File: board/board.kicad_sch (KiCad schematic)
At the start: 4 parts, among them J1 0xx_LED, J2 0xx_LED

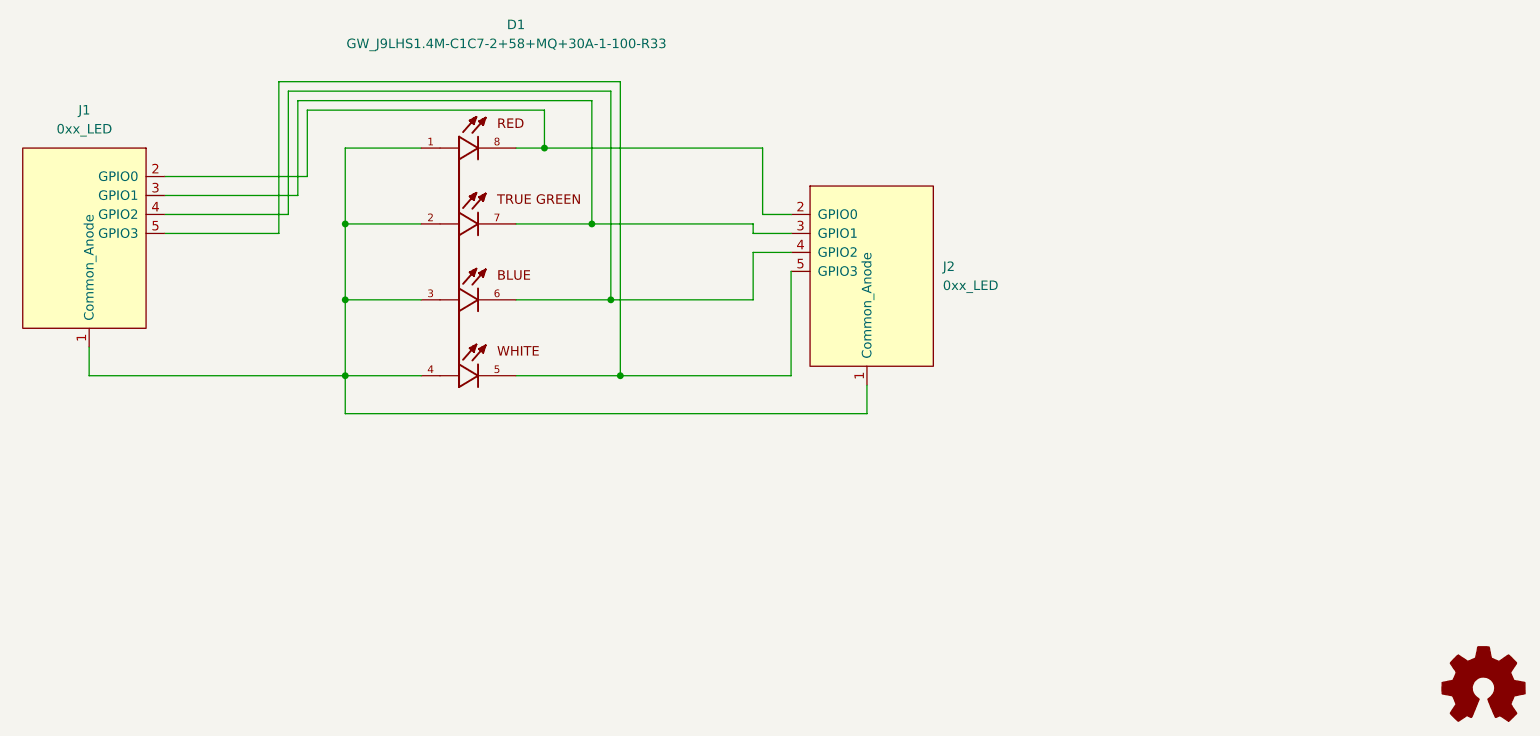
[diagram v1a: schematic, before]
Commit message: Update Layout | Remove DRC Errors | Connected unused Edgy Pins
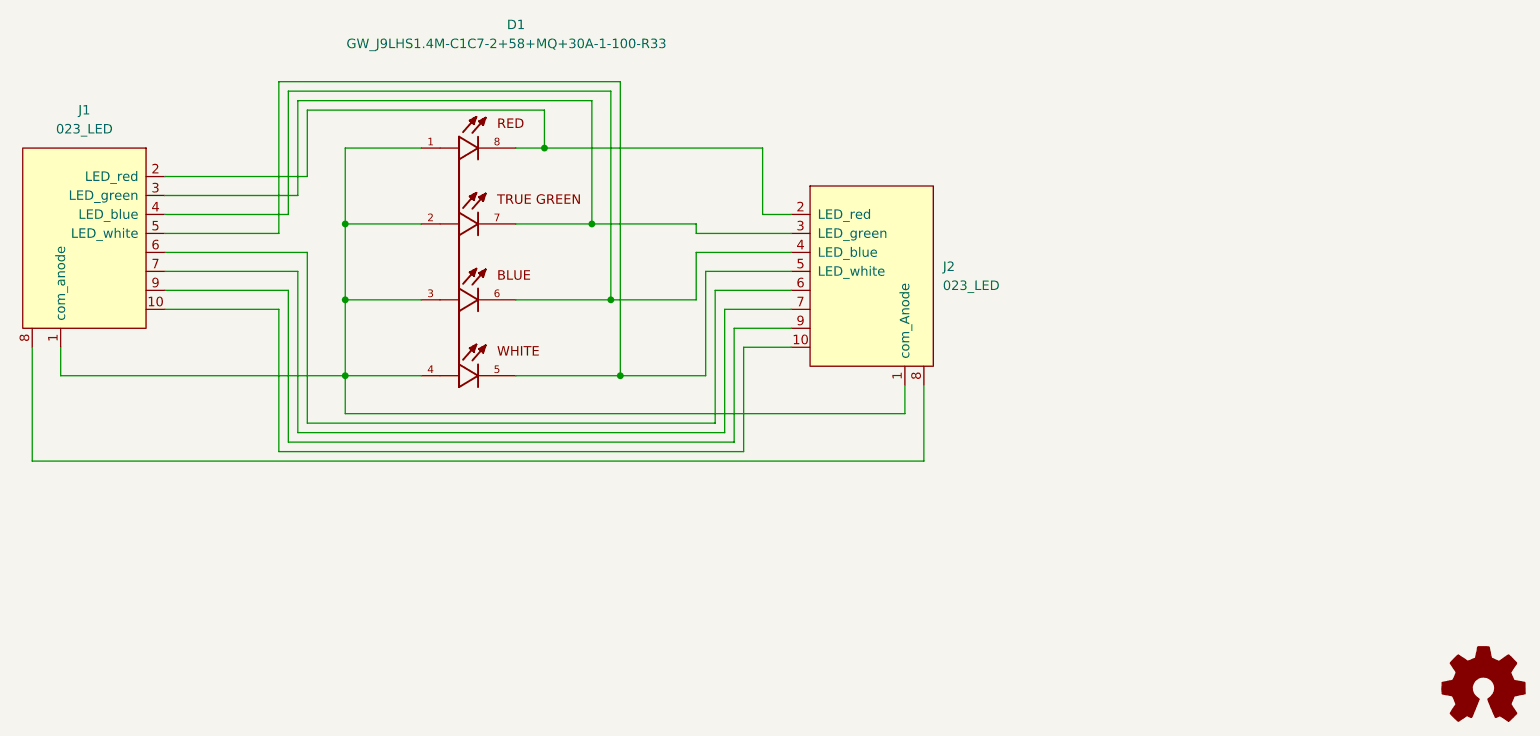
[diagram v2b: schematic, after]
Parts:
- J1, J2: value 0xx_LED -> 023_LED
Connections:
- new net: J1.10, J2.10
- new net: J1.6, J2.6
- new net: J1.7, J2.7
- new net: J1.8, J2.8
- new net: J1.9, J2.9
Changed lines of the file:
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@@
   (junction (at 153.67 95.25) (diameter 0) (color 0 0 0 0)
   )
+  (junction (at 157.48 115.57) (diameter 0) (color 0 0 0 0)
+  )
   (junction (at 147.32 85.09) (diameter 0) (color 0 0 0 0)
   )
   (junction (at 120.65 105.41) (diameter 0) (color 0 0 0 0)
   )
-  (junction (at 157.48 115.57) (diameter 0) (color 0 0 0 0)
-  )
-  (wire (pts (xy 86.36 115.57) (xy 120.65 115.57))
+  (wire (pts (xy 96.52 99.06) (xy 115.57 99.06))
+    (stroke (width 0) (type default) (color 0 0 0 0))
+  )
+  (wire (pts (xy 82.55 115.57) (xy 120.65 115.57))
+    (stroke (width 0) (type default) (color 0 0 0 0))
+  )
+  (wire (pts (xy 168.91 101.6) (xy 180.34 101.6))
     (stroke (width 0) (type default) (color 0 0 0 0))
   )
@@
     (stroke (width 0) (type default) (color 0 0 0 0))
   )
+  (wire (pts (xy 172.72 124.46) (xy 172.72 109.22))
+    (stroke (width 0) (type default) (color 0 0 0 0))
+  )
   (wire (pts (xy 147.32 85.09) (xy 147.32 80.01))
     (stroke (width 0) (type default) (color 0 0 0 0))
@@
     (stroke (width 0) (type default) (color 0 0 0 0))
   )
-  (wire (pts (xy 190.5 116.84) (xy 190.5 120.65))
+  (wire (pts (xy 195.58 116.84) (xy 195.58 120.65))
+    (stroke (width 0) (type default) (color 0 0 0 0))
+  )
+  (wire (pts (xy 115.57 121.92) (xy 170.18 121.92))
     (stroke (width 0) (type default) (color 0 0 0 0))
   )
@@
     (stroke (width 0) (type default) (color 0 0 0 0))
   )
-  (wire (pts (xy 180.34 96.52) (xy 175.26 96.52))
+  (wire (pts (xy 168.91 101.6) (xy 168.91 115.57))
+    (stroke (width 0) (type default) (color 0 0 0 0))
+  )
+  (wire (pts (xy 180.34 96.52) (xy 167.64 96.52))
     (stroke (width 0) (type default) (color 0 0 0 0))
   )
@@
     (stroke (width 0) (type default) (color 0 0 0 0))
   )
-  (wire (pts (xy 180.34 99.06) (xy 175.26 99.06))
+  (wire (pts (xy 180.34 99.06) (xy 167.64 99.06))
     (stroke (width 0) (type default) (color 0 0 0 0))
   )
@@
     (stroke (width 0) (type default) (color 0 0 0 0))
   )
-  (wire (pts (xy 175.26 95.25) (xy 153.67 95.25))
+  (wire (pts (xy 167.64 95.25) (xy 153.67 95.25))
+    (stroke (width 0) (type default) (color 0 0 0 0))
+  )
+  (wire (pts (xy 172.72 109.22) (xy 180.34 109.22))
     (stroke (width 0) (type default) (color 0 0 0 0))
   )
@@
     (stroke (width 0) (type default) (color 0 0 0 0))
   )
-  (wire (pts (xy 180.34 115.57) (xy 157.48 115.57))
-    (stroke (width 0) (type default) (color 0 0 0 0))
-  )
-  (wire (pts (xy 120.65 120.65) (xy 190.5 120.65))
+  (wire (pts (xy 120.65 120.65) (xy 195.58 120.65))
     (stroke (width 0) (type default) (color 0 0 0 0))
   )
@@
     (stroke (width 0) (type default) (color 0 0 0 0))
   )
+  (wire (pts (xy 96.52 104.14) (xy 113.03 104.14))
+    (stroke (width 0) (type default) (color 0 0 0 0))
+  )
+  (wire (pts (xy 114.3 123.19) (xy 114.3 101.6))
+    (stroke (width 0) (type default) (color 0 0 0 0))
+  )
+  (wire (pts (xy 113.03 104.14) (xy 113.03 124.46))
+    (stroke (width 0) (type default) (color 0 0 0 0))
+  )
   (wire (pts (xy 130.81 85.09) (xy 120.65 85.09))
     (stroke (width 0) (type default) (color 0 0 0 0))
   )
+  (wire (pts (xy 171.45 123.19) (xy 114.3 123.19))
+    (stroke (width 0) (type default) (color 0 0 0 0))
+  )
   (wire (pts (xy 176.53 93.98) (xy 176.53 85.09))
     (stroke (width 0) (type default) (color 0 0 0 0))
   )
+  (wire (pts (xy 115.57 99.06) (xy 115.57 121.92))
+    (stroke (width 0) (type default) (color 0 0 0 0))
+  )
+  (wire (pts (xy 78.74 127) (xy 198.12 127))
+    (stroke (width 0) (type default) (color 0 0 0 0))
+  )
   (wire (pts (xy 96.52 91.44) (xy 114.3 91.44))
     (stroke (width 0) (type default) (color 0 0 0 0))
   )
+  (wire (pts (xy 198.12 127) (xy 198.12 116.84))
+    (stroke (width 0) (type default) (color 0 0 0 0))
+  )
+  (wire (pts (xy 180.34 104.14) (xy 170.18 104.14))
+    (stroke (width 0) (type default) (color 0 0 0 0))
+  )
+  (wire (pts (xy 111.76 125.73) (xy 111.76 106.68))
+    (stroke (width 0) (type default) (color 0 0 0 0))
+  )
   (wire (pts (xy 180.34 93.98) (xy 176.53 93.98))
     (stroke (width 0) (type default) (color 0 0 0 0))
   )
+  (wire (pts (xy 78.74 111.76) (xy 78.74 127))
+    (stroke (width 0) (type default) (color 0 0 0 0))
+  )
   (wire (pts (xy 114.3 78.74) (xy 153.67 78.74))
     (stroke (width 0) (type default) (color 0 0 0 0))
@@
     (stroke (width 0) (type default) (color 0 0 0 0))
   )
-  (wire (pts (xy 175.26 96.52) (xy 175.26 95.25))
+  (wire (pts (xy 167.64 96.52) (xy 167.64 95.25))
+    (stroke (width 0) (type default) (color 0 0 0 0))
+  )
+  (wire (pts (xy 173.99 111.76) (xy 173.99 125.73))
     (stroke (width 0) (type default) (color 0 0 0 0))
   )
@@
     (stroke (width 0) (type default) (color 0 0 0 0))
   )
-  (wire (pts (xy 180.34 101.6) (xy 180.34 115.57))
-    (stroke (width 0) (type default) (color 0 0 0 0))
-  )
-  (wire (pts (xy 86.36 111.76) (xy 86.36 115.57))
+  (wire (pts (xy 114.3 101.6) (xy 96.52 101.6))
+    (stroke (width 0) (type default) (color 0 0 0 0))
+  )
+  (wire (pts (xy 82.55 111.76) (xy 82.55 115.57))
     (stroke (width 0) (type default) (color 0 0 0 0))
   )
@@
     (stroke (width 0) (type default) (color 0 0 0 0))
   )
+  (wire (pts (xy 173.99 125.73) (xy 111.76 125.73))
+    (stroke (width 0) (type default) (color 0 0 0 0))
+  )
   (wire (pts (xy 156.21 105.41) (xy 156.21 77.47))
     (stroke (width 0) (type default) (color 0 0 0 0))
@@
     (stroke (width 0) (type default) (color 0 0 0 0))
   )
+  (wire (pts (xy 170.18 104.14) (xy 170.18 121.92))
+    (stroke (width 0) (type default) (color 0 0 0 0))
+  )
+  (wire (pts (xy 171.45 106.68) (xy 171.45 123.19))
+    (stroke (width 0) (type default) (color 0 0 0 0))
+  )
   (wire (pts (xy 115.57 80.01) (xy 115.57 88.9))
     (stroke (width 0) (type default) (color 0 0 0 0))
   )
+  (wire (pts (xy 111.76 106.68) (xy 96.52 106.68))
+    (stroke (width 0) (type default) (color 0 0 0 0))
+  )
   (wire (pts (xy 147.32 80.01) (xy 115.57 80.01))
     (stroke (width 0) (type default) (color 0 0 0 0))
@@
     (stroke (width 0) (type default) (color 0 0 0 0))
   )
-  (wire (pts (xy 175.26 99.06) (xy 175.26 105.41))
+  (wire (pts (xy 167.64 99.06) (xy 167.64 105.41))
+    (stroke (width 0) (type default) (color 0 0 0 0))
+  )
+  (wire (pts (xy 180.34 106.68) (xy 171.45 106.68))
     (stroke (width 0) (type default) (color 0 0 0 0))
   )
@@
     (stroke (width 0) (type default) (color 0 0 0 0))
   )
+  (wire (pts (xy 168.91 115.57) (xy 157.48 115.57))
+    (stroke (width 0) (type default) (color 0 0 0 0))
+  )
+  (wire (pts (xy 113.03 124.46) (xy 172.72 124.46))
+    (stroke (width 0) (type default) (color 0 0 0 0))
+  )
   (wire (pts (xy 120.65 95.25) (xy 130.81 95.25))
     (stroke (width 0) (type default) (color 0 0 0 0))
@@
     (stroke (width 0) (type default) (color 0 0 0 0))
   )
-  (wire (pts (xy 175.26 105.41) (xy 156.21 105.41))
+  (wire (pts (xy 167.64 105.41) (xy 156.21 105.41))
+    (stroke (width 0) (type default) (color 0 0 0 0))
+  )
+  (wire (pts (xy 180.34 111.76) (xy 173.99 111.76))
     (stroke (width 0) (type default) (color 0 0 0 0))
   )
@@
     (in_bom yes) (on_board yes) (fields_autoplaced)
     (property "Reference" "J1" (id 0) (at 85.725 80.01 0))
-    (property "Value" "0xx_LED" (id 1) (at 85.725 82.55 0))
+    (property "Value" "023_LED" (id 1) (at 85.725 82.55 0))
     (property "Footprint" "on_edge:on_edge_2x05_device" (id 2) (at 77.47 81.28 0)
       (effects (font (size 1.27 1.27)) hide)
@@
     (pin "4")
     (pin "5")
+    (pin "8")
+    (pin "6")
+    (pin "7")
+    (pin "9")
+    (pin "10")
   )
   (symbol (lib_id "put_on_edge:011_GPIO") (at 191.77 102.87 0) (unit 1)
@@
       (effects (font (size 1.27 1.27)) (justify left))
     )
-    (property "Value" "0xx_LED" (id 1) (at 200.66 103.5049 0)
+    (property "Value" "023_LED" (id 1) (at 200.66 103.5049 0)
       (effects (font (size 1.27 1.27)) (justify left))
     )
@@
     )
     (pin "1")
+    (pin "10")
     (pin "2")
     (pin "3")
     (pin "4")
     (pin "5")
+    (pin "6")
+    (pin "7")
+    (pin "8")
+    (pin "9")
   )
   (symbol (lib_id "GW_J9LHS1.4M-C1C7-2_58_MQ_30A-1-100-R33:GW_J9LHS1.4M-C1C7-2+58+MQ+30A-1-100-R33") (at 138.43 100.33 0) (unit 1)
@@
     )
     (path "/02ab4736-fba1-4e6c-abef-aa7c088d94a7"
-      (reference "J1") (unit 1) (value "0xx_LED") (footprint "on_edge:on_edge_2x05_device")
+      (reference "J1") (unit 1) (value "023_LED") (footprint "on_edge:on_edge_2x05_device")
     )
     (path "/6169c5fa-dc29-45cd-8d2f-b575e54f7735"
-      (reference "J2") (unit 1) (value "0xx_LED") (footprint "on_edge:on_edge_2x05_host")
+      (reference "J2") (unit 1) (value "023_LED") (footprint "on_edge:on_edge_2x05_host")
     )
     (path "/b72b6f4a-7489-40f2-bb90-d75ae01aa368"

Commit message: Change edgy connector back to GPIO | Began adding Resistor to specific voltage
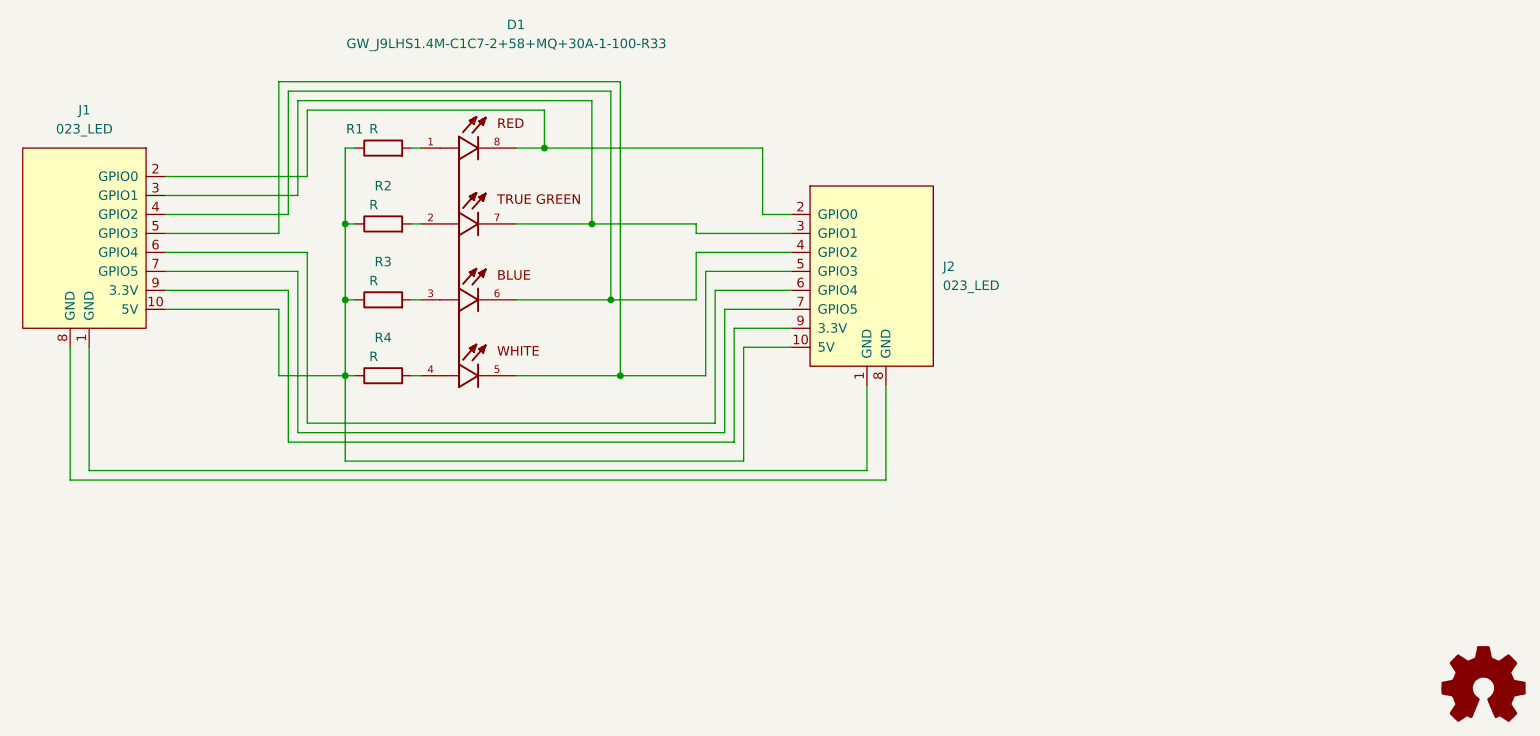
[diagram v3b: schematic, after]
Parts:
- added R1, R2, R3, R4: R, Resistor_SMD:R_0603_1608Metric_Pad0.98x0.95mm_HandSolder, symbol Device:R
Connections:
- net at J1.10 (5V), J2.10 (5V): now also R1.1, R2.1, R3.1, R4.1
- new net: J1.1 (GND), J2.1 (GND)
- new net: D1.3, R3.2
- new net: D1.1, R1.2
- new net: D1.2, R2.2
- new net: D1.4, R4.2

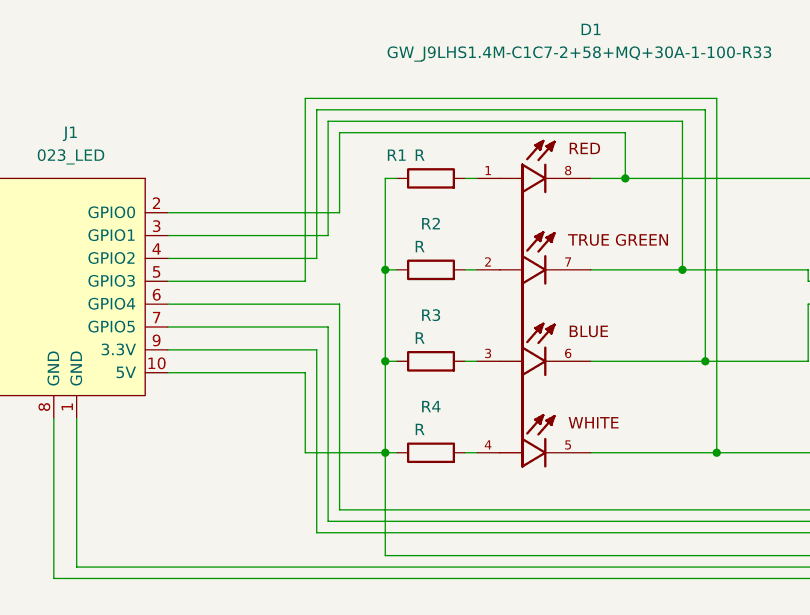
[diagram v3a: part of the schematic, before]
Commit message: Add value to resistor
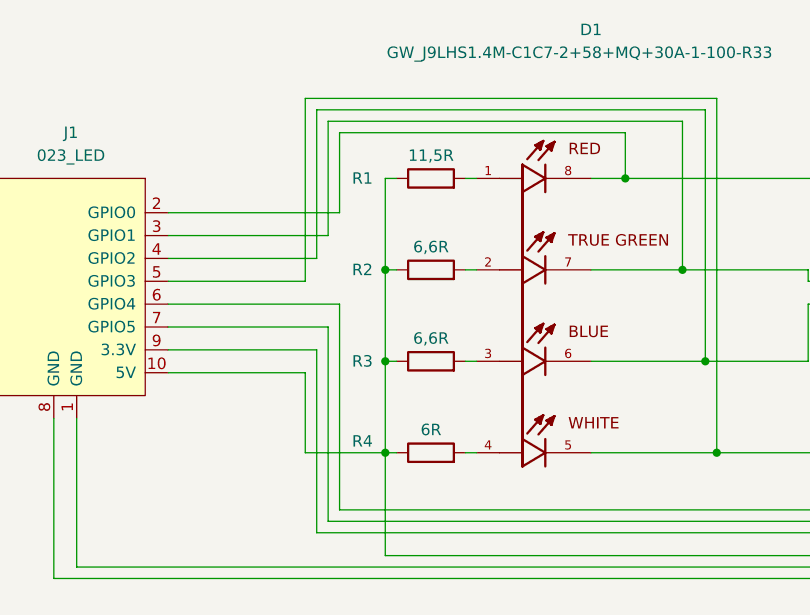
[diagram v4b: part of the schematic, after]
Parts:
- R1: value R -> 11,5R; footprint Resistor_SMD:R_0603_1608Metric_Pad0.98x0.95mm_HandSolder -> Resistor_SMD:R_0805_2012Metric_Pad1.20x1.40mm_HandSolder
- R2, R3: value R -> 6,6R
- R4: value R -> 6R
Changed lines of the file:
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@@
   (symbol (lib_id "Device:R") (at 125.73 105.41 90) (unit 1)
     (in_bom yes) (on_board yes)
-    (property "Reference" "R3" (id 0) (at 125.73 100.33 90))
-    (property "Value" "R" (id 1) (at 124.46 102.87 90))
+    (property "Reference" "R3" (id 0) (at 118.11 105.41 90))
+    (property "Value" "6,6R" (id 1) (at 125.73 102.87 90))
     (property "Footprint" "Resistor_SMD:R_0603_1608Metric_Pad0.98x0.95mm_HandSolder" (id 2) (at 125.73 107.188 90)
       (effects (font (size 1.27 1.27)) hide)
@@
   (symbol (lib_id "Device:R") (at 125.73 85.09 90) (unit 1)
     (in_bom yes) (on_board yes)
-    (property "Reference" "R1" (id 0) (at 121.92 82.55 90))
-    (property "Value" "R" (id 1) (at 124.46 82.55 90))
-    (property "Footprint" "Resistor_SMD:R_0603_1608Metric_Pad0.98x0.95mm_HandSolder" (id 2) (at 125.73 86.868 90)
+    (property "Reference" "R1" (id 0) (at 118.11 85.09 90))
+    (property "Value" "11,5R" (id 1) (at 125.73 82.55 90))
+    (property "Footprint" "Resistor_SMD:R_0805_2012Metric_Pad1.20x1.40mm_HandSolder" (id 2) (at 125.73 86.868 90)
       (effects (font (size 1.27 1.27)) hide)
     )
@@
   (symbol (lib_id "Device:R") (at 125.73 95.25 90) (unit 1)
     (in_bom yes) (on_board yes)
-    (property "Reference" "R2" (id 0) (at 125.73 90.17 90))
-    (property "Value" "R" (id 1) (at 124.46 92.71 90))
+    (property "Reference" "R2" (id 0) (at 118.11 95.25 90))
+    (property "Value" "6,6R" (id 1) (at 125.73 92.71 90))
     (property "Footprint" "Resistor_SMD:R_0603_1608Metric_Pad0.98x0.95mm_HandSolder" (id 2) (at 125.73 97.028 90)
       (effects (font (size 1.27 1.27)) hide)
@@
   (symbol (lib_id "Device:R") (at 125.73 115.57 90) (unit 1)
     (in_bom yes) (on_board yes)
-    (property "Reference" "R4" (id 0) (at 125.73 110.49 90))
-    (property "Value" "R" (id 1) (at 124.46 113.03 90))
+    (property "Reference" "R4" (id 0) (at 118.11 114.3 90))
+    (property "Value" "6R" (id 1) (at 125.73 113.03 90))
     (property "Footprint" "Resistor_SMD:R_0603_1608Metric_Pad0.98x0.95mm_HandSolder" (id 2) (at 125.73 117.348 90)
       (effects (font (size 1.27 1.27)) hide)
@@
     )
     (path "/27ab3316-53c1-4160-b7ca-0005b905f6e7"
-      (reference "R1") (unit 1) (value "R") (footprint "Resistor_SMD:R_0603_1608Metric_Pad0.98x0.95mm_HandSolder")
+      (reference "R1") (unit 1) (value "11,5R") (footprint "Resistor_SMD:R_0805_2012Metric_Pad1.20x1.40mm_HandSolder")
     )
     (path "/308cc854-65fc-4285-89fd-abe8c5bd7555"
-      (reference "R2") (unit 1) (value "R") (footprint "Resistor_SMD:R_0603_1608Metric_Pad0.98x0.95mm_HandSolder")
+      (reference "R2") (unit 1) (value "6,6R") (footprint "Resistor_SMD:R_0603_1608Metric_Pad0.98x0.95mm_HandSolder")
     )
     (path "/218c726d-046f-4365-a5e8-1950dceb4511"
-      (reference "R3") (unit 1) (value "R") (footprint "Resistor_SMD:R_0603_1608Metric_Pad0.98x0.95mm_HandSolder")
+      (reference "R3") (unit 1) (value "6,6R") (footprint "Resistor_SMD:R_0603_1608Metric_Pad0.98x0.95mm_HandSolder")
     )
     (path "/65e7f034-4b17-4c4e-ad56-1a953a5e983d"
-      (reference "R4") (unit 1) (value "R") (footprint "Resistor_SMD:R_0603_1608Metric_Pad0.98x0.95mm_HandSolder")
+      (reference "R4") (unit 1) (value "6R") (footprint "Resistor_SMD:R_0603_1608Metric_Pad0.98x0.95mm_HandSolder")
     )
   )
